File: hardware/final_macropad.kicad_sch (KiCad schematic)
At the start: 65 parts, among them J1 OLED_128x64, SW1 SW_Push, U1 ATmega32U4-A, Y1 16MHz

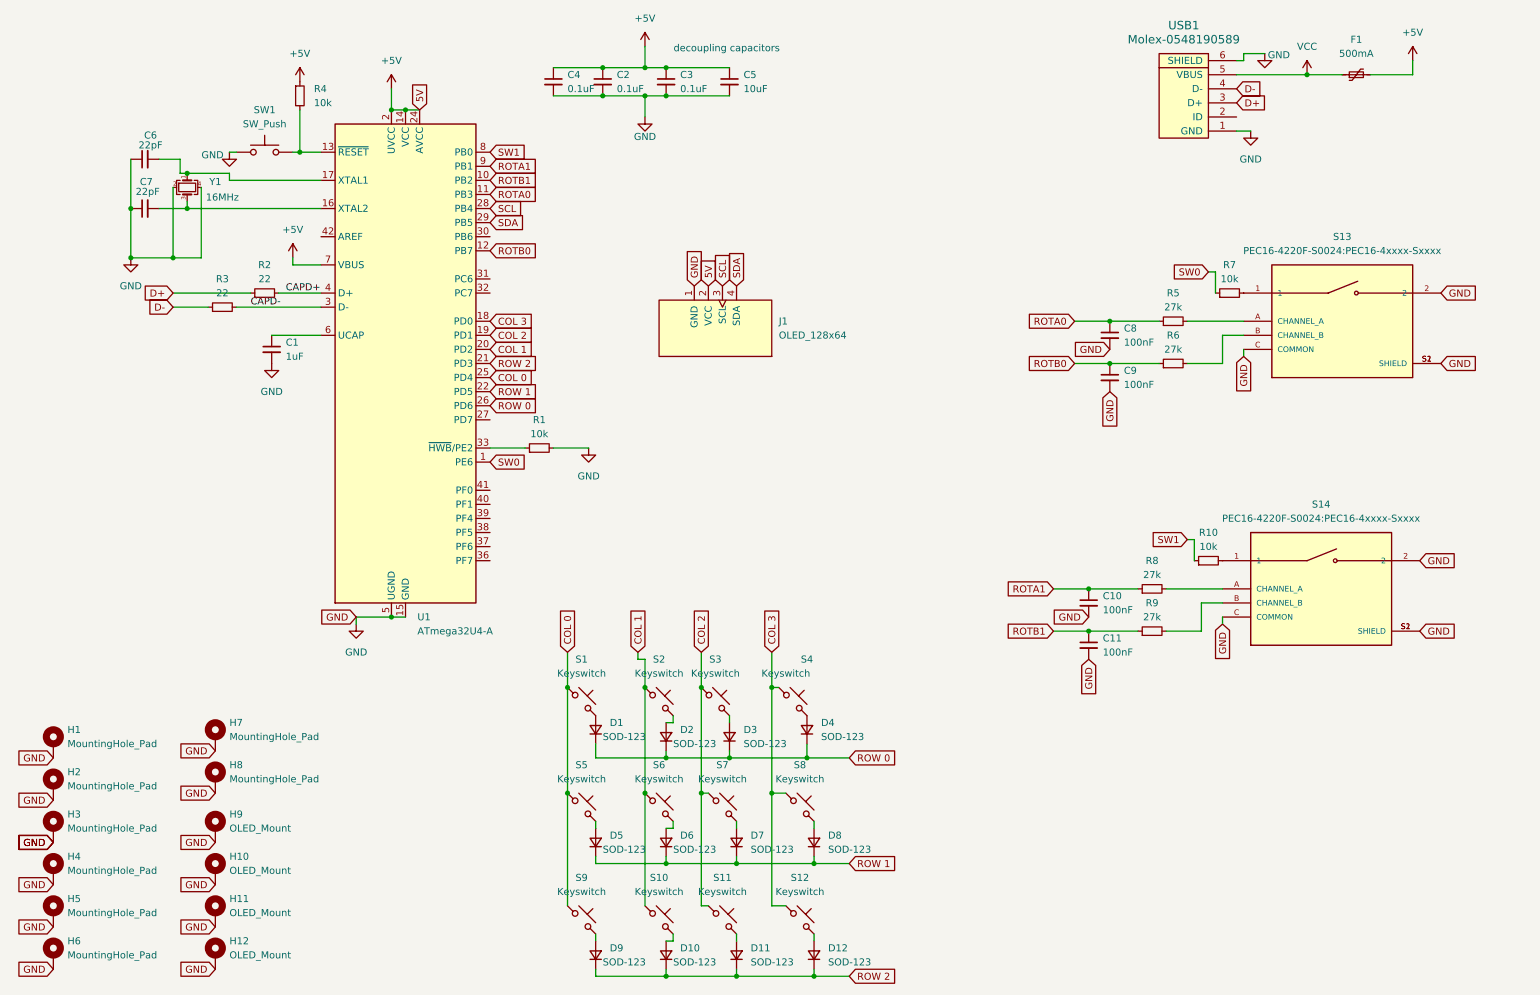
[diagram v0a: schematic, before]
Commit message: organize schematic and add USB-C and surge protector
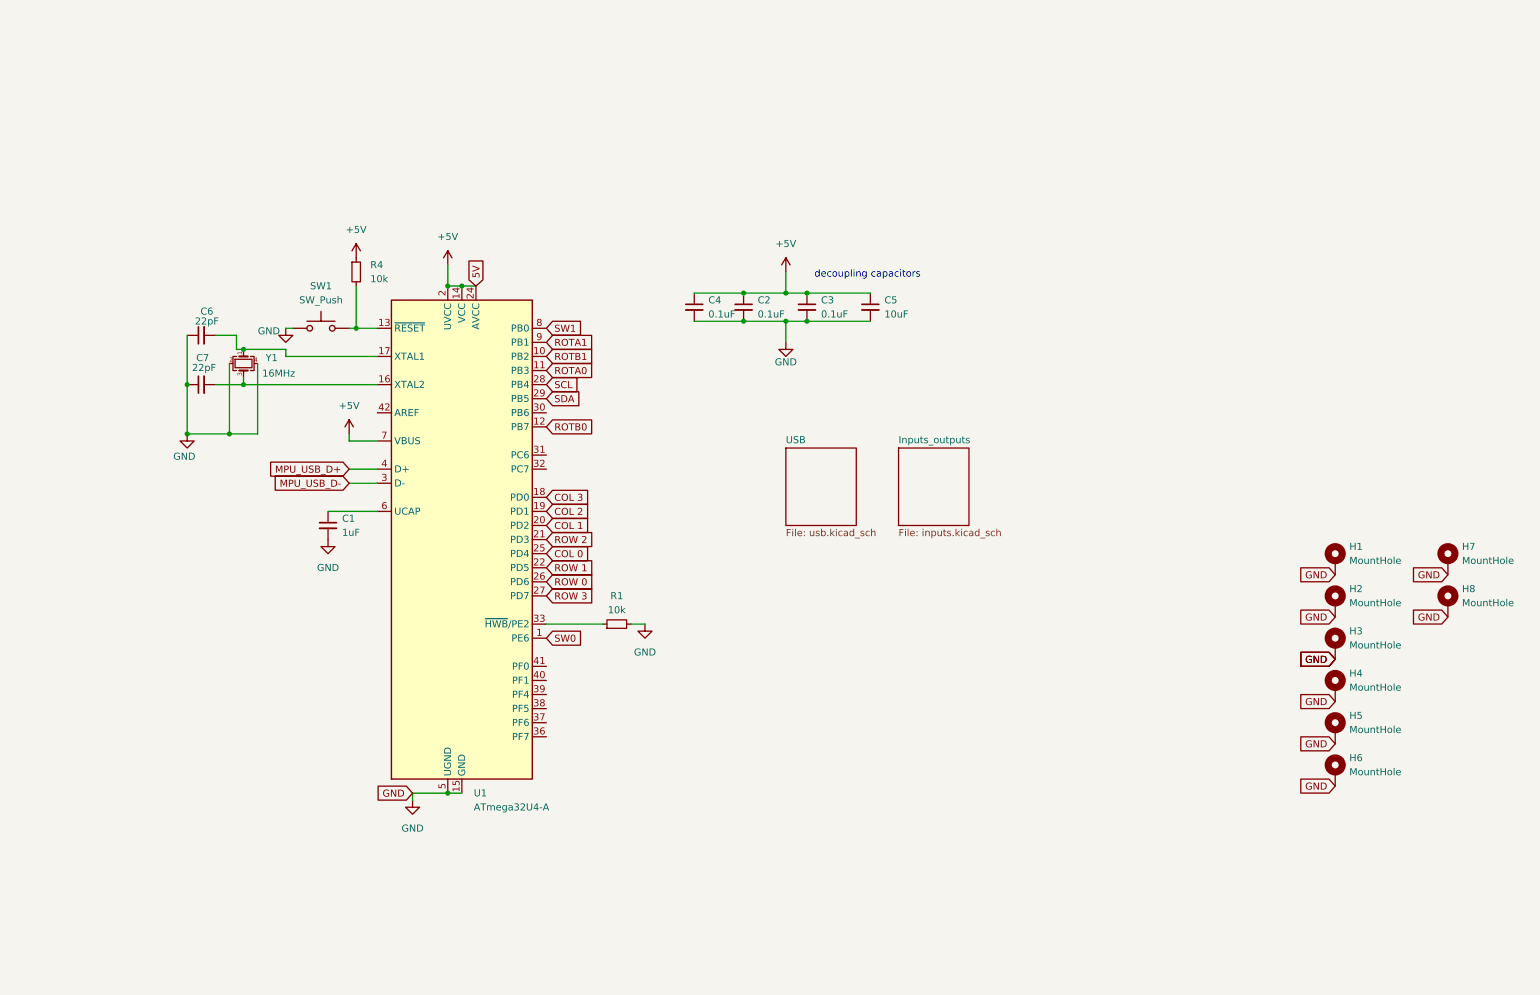
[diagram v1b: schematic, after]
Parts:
- removed C10, C11, C8, C9: 100nF, Capacitor_SMD:C_0805_2012Metric, symbol Device:C_Small
- removed D1, D10, D11, D12, D2, D3, D4, D5, D6, D7, D8, D9: SOD-123, Diode_SMD:D_SOD-123, symbol Device:D_Small
- removed F1: 500mA, Fuse:Fuse_1206_3216Metric, symbol Device:Polyfuse_Small
- removed H10, H11, H12, H9: OLED_Mount, MountingHole:MountingHole_2.2mm_M2_Pad, symbol Mechanical:MountingHole_Pad
- removed J1: OLED_128x64, ScottoKeebs_Components:OLED_128x64, symbol ScottoKeebs:OLED_128x64
- removed R10, R7: 10k, Resistor_SMD:R_0805_2012Metric, symbol Device:R_Small
- removed R2, R3: 22, Resistor_SMD:R_0402_1005Metric_Pad0.72x0.64mm_HandSolder, symbol Device:R_Small
- removed R5, R6, R8, R9: 27k, Resistor_SMD:R_0805_2012Metric, symbol Device:R_Small
- removed S1, S10, S11, S12, S2, S3, S4, S5, S6, S7, S8, S9: Keyswitch, Button_Switch_Keyboard:SW_Cherry_MX_1.00u_PCB, symbol ScottoKeebs:Placeholder_Keyswitch
- removed S13: PEC16-4220F-S0024:PEC16-4xxxx-Sxxxx, PEC16-4220F-S0024:PEC16-4xxxx-Sxxxx, symbol PEC12R-2220F-S0024:PEC12R-2220F-S0024
- removed S14: PEC16-4220F-S0024:PEC16-4xxxx-Sxxxx, kicad-footprints:PEC16-4xxxx-Sxxxx, symbol PEC12R-2220F-S0024:PEC12R-2220F-S0024
- removed USB1: Molex-0548190589, random-keyboard-parts:Molex-0548190589, symbol random-keyboard-parts:Molex-0548190589
- H1, H2, H3, H4, H5, H6, H7, H8: value MountingHole_Pad -> MountHole
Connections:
- net ROW 3: now reaches U1.27 (PD7)
- net CAPD+ renamed MPU_USB_D+
- net CAPD- renamed MPU_USB_D-
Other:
- added sheet Inputs_outputs (inputs.kicad_sch)
- added sheet USB (usb.kicad_sch)
- moved on the sheet: C1, C2, C3, C4, C5, C6, C7, H1, H2, H3, H4, H5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

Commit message: fix switches to be correct order and move diodes
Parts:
- H5, H6, H7, H8: footprint MountingHole:MountingHole_3.2mm_M3_Pad_Via -> MountingHole:MountingHole_2.2mm_M2_Pad
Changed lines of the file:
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@@
 			)
 		)
-		(property "Footprint" "MountingHole:MountingHole_3.2mm_M3_Pad_Via"
+		(property "Footprint" "MountingHole:MountingHole_2.2mm_M2_Pad"
 			(at 251.46 146.05 0)
 			(effects
@@
 			)
 		)
-		(property "Footprint" "MountingHole:MountingHole_3.2mm_M3_Pad_Via"
+		(property "Footprint" "MountingHole:MountingHole_2.2mm_M2_Pad"
 			(at 271.78 123.19 0)
 			(effects
@@
 			)
 		)
-		(property "Footprint" "MountingHole:MountingHole_3.2mm_M3_Pad_Via"
+		(property "Footprint" "MountingHole:MountingHole_2.2mm_M2_Pad"
 			(at 251.46 153.67 0)
 			(effects
@@
 			)
 		)
-		(property "Footprint" "MountingHole:MountingHole_3.2mm_M3_Pad_Via"
+		(property "Footprint" "MountingHole:MountingHole_2.2mm_M2_Pad"
 			(at 271.78 115.57 0)
 			(effects

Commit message: update BOM and reset button footprint
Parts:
- removed SW1: SW_Push, random-keyboard-parts:SKQG-1155865, symbol Switch:SW_Push
- added SW1: SKQGADE010, SKQGADE010_AAL, symbol low_profile_switch_4809-SKQGADE010:SKQGADE010
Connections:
- net GND: now also SW1.4
- net at R4.2, U1.13 (~{RESET}): now also SW1.3
- no-connect marks 0 -> 10
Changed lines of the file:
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@@
 		(color 0 0 0 0)
 	)
+	(no_connect
+		(at 109.22 134.62)
+	)
+	(no_connect
+		(at 109.22 142.24)
+	)
+	(no_connect
+		(at 109.22 139.7)
+	)
+	(no_connect
+		(at 43.18 66.04)
+	)
+	(no_connect
+		(at 109.22 99.06)
+	)
+	(no_connect
+		(at 109.22 147.32)
+	)
+	(no_connect
+		(at 68.58 66.04)
+	)
+	(no_connect
+		(at 109.22 96.52)
+	)
+	(no_connect
+		(at 109.22 137.16)
+	)
+	(no_connect
+		(at 109.22 144.78)
+	)
 	(wire
 		(pts
@@
 	(wire
 		(pts
+			(xy 71.12 73.66) (xy 71.12 63.5)
+		)
+		(stroke
+			(width 0)
+			(type default)
+		)
+	)
+	(wire
+		(pts
 			(xy 49.53 83.82) (xy 54.61 83.82)
 		)
@@
 	(wire
 		(pts
-			(xy 73.66 73.66) (xy 74.93 73.66)
+			(xy 71.12 73.66) (xy 74.93 73.66)
 		)
 		(stroke
@@
 	(wire
 		(pts
+			(xy 71.12 63.5) (xy 68.58 63.5)
+		)
+		(stroke
+			(width 0)
+			(type default)
+		)
+	)
+	(wire
+		(pts
 			(xy 62.23 78.74) (xy 62.23 77.47)
 		)
@@
 	(wire
 		(pts
-			(xy 63.5 73.66) (xy 62.23 73.66)
-		)
-		(stroke
-			(width 0)
-			(type default)
-		)
-	)
-	(wire
-		(pts
 			(xy 85.09 158.75) (xy 85.09 157.48)
 		)
@@
 		(pts
 			(xy 62.23 78.74) (xy 78.74 78.74)
+		)
+		(stroke
+			(width 0)
+			(type default)
+		)
+	)
+	(wire
+		(pts
+			(xy 40.64 63.5) (xy 43.18 63.5)
 		)
 		(stroke
@@
 	(symbol
 		(lib_id "power:GND")
-		(at 62.23 73.66 0)
+		(at 40.64 63.5 0)
 		(unit 1)
 		(exclude_from_sim no)
@@
 		(dnp no)
 		(property "Reference" "#PWR09"
-			(at 62.23 80.01 0)
+			(at 40.64 69.85 0)
 			(effects
 				(font
@@
 		)
 		(property "Value" "GND"
-			(at 59.182 74.168 0)
+			(at 37.592 64.008 0)
 			(effects
 				(font
@@
 		)
 		(property "Footprint" ""
-			(at 62.23 73.66 0)
+			(at 40.64 63.5 0)
 			(effects
 				(font
@@
 		)
 		(property "Datasheet" ""
-			(at 62.23 73.66 0)
+			(at 40.64 63.5 0)
 			(effects
 				(font
@@
 		)
 		(property "Description" "Power symbol creates a global label with name \"GND\" , ground"
-			(at 62.23 73.66 0)
+			(at 40.64 63.5 0)
 			(effects
 				(font
@@
 	)
 	(symbol
-		(lib_id "Switch:SW_Push")
-		(at 68.58 73.66 0)
-		(unit 1)
-		(exclude_from_sim no)
-		(in_bom yes)
-		(on_board yes)
-		(dnp no)
-		(fields_autoplaced yes)
-		(property "Reference" "SW1"
-			(at 68.58 66.04 0)
-			(effects
-				(font
-					(size 1.27 1.27)
-				)
-			)
-		)
-		(property "Value" "SW_Push"
-			(at 68.58 68.58 0)
-			(effects
-				(font
-					(size 1.27 1.27)
-				)
-			)
-		)
-		(property "Footprint" "random-keyboard-parts:SKQG-1155865"
-			(at 68.58 68.58 0)
-			(effects
-				(font
-					(size 1.27 1.27)
-				)
-				(hide yes)
-			)
-		)
-		(property "Datasheet" "~"
-			(at 68.58 68.58 0)
-			(effects
-				(font
-					(size 1.27 1.27)
-				)
-				(hide yes)
-			)
-		)
-		(property "Description" "Push button switch, generic, two pins"
-			(at 68.58 73.66 0)
-			(effects
-				(font
-					(size 1.27 1.27)
-				)
-				(hide yes)
-			)
-		)
-		(pin "1"
-		)
-		(pin "2"
-		)
-		(instances
-			(project "final_macropad"
-				(path "/5d184ef1-151a-4114-9d49-de87ac832ddf"
-					(reference "SW1")
-					(unit 1)
-				)
-			)
-		)
-	)
-	(symbol
 		(lib_id "Mechanical:MountingHole_Pad")
 		(at 251.46 146.05 0)
@@
 					(unit 1)
 				)
+			)
+		)
+	)
+	(symbol
+		(lib_id "low_profile_switch_4809-SKQGADE010:SKQGADE010")
+		(at 68.58 66.04 180)
+		(unit 1)
+		(exclude_from_sim no)
+		(in_bom yes)
+		(on_board yes)
+		(dnp no)
+		(fields_autoplaced yes)
+		(property "Reference" "SW1"
+			(at 55.88 55.88 0)
+			(effects
+				(font
+					(size 1.524 1.524)
+				)
+			)
+		)
+		(property "Value" "SKQGADE010"
+			(at 55.88 58.42 0)
+			(effects
+				(font
+					(size 1.524 1.524)
+				)
+			)
+		)
+		(property "Footprint" "SKQGADE010_AAL"
+			(at 68.58 66.04 0)
+			(effects
+				(font
+					(size 1.27 1.27)
+					(italic yes)
+				)
+				(hide yes)
+			)
+		)
+		(property "Datasheet" "SKQGADE010"
+			(at 68.58 66.04 0)
+			(effects
+				(font
+					(size 1.27 1.27)
+					(italic yes)
+				)
+				(hide yes)
+			)
+		)
+		(property "Description" ""
+			(at 68.58 66.04 0)
+			(effects
+				(font
+					(size 1.27 1.27)
+				)
+				(hide yes)
+			)
+		)
+		(pin "1"
+		)
+		(pin "3"
+		)
+		(pin "2"
+		)
+		(pin "4"
+		)
+		(instances
+			(project ""
+				(path "/5d184ef1-151a-4114-9d49-de87ac832ddf"
+					(reference "SW1")
+					(unit 1)
+				)

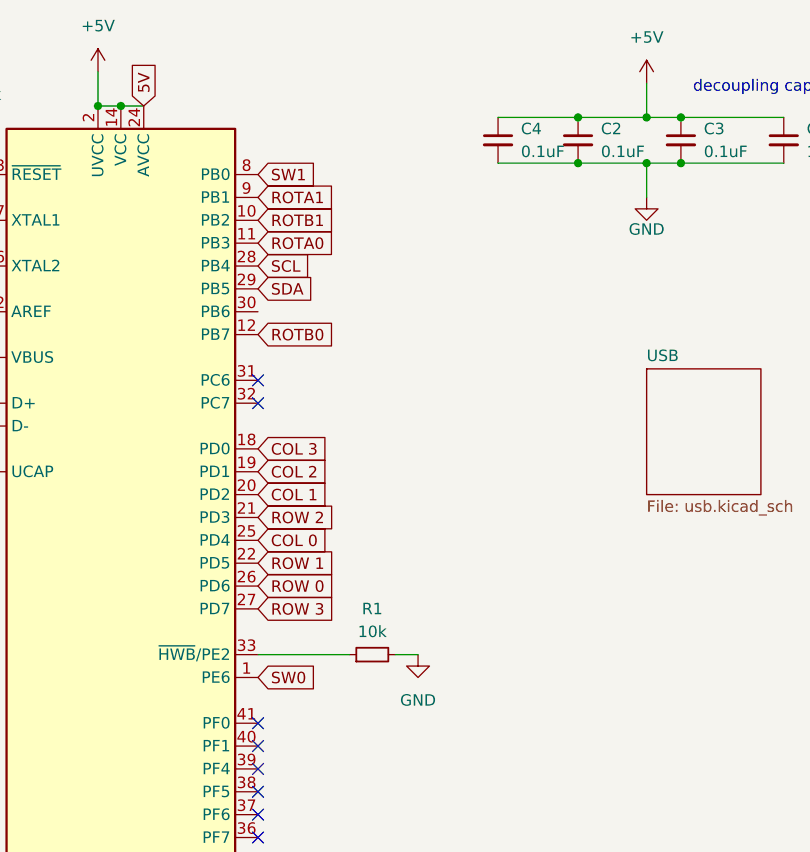
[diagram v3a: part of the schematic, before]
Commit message: rotate MCU, route reset button, crystal, and OLED
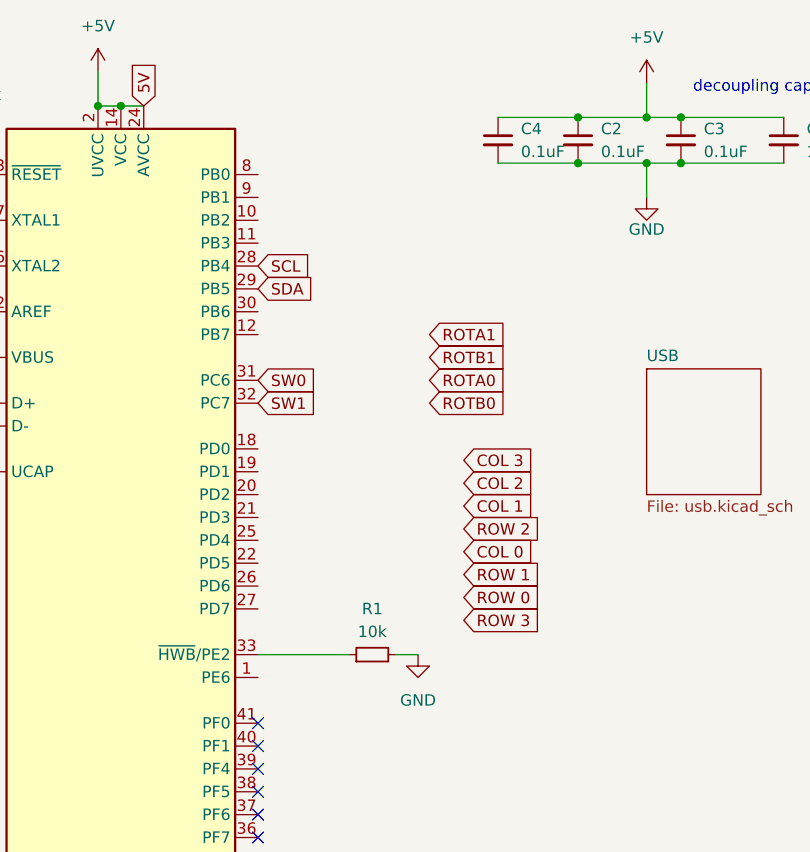
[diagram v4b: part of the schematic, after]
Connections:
- net COL 0: no longer U1.25 (PD4)
- net COL 1: no longer U1.20 (PD2)
- net COL 2: no longer U1.19 (PD1)
- net COL 3: no longer U1.18 (PD0)
- net ROTA0: no longer U1.11 (PB3)
- net ROTA1: no longer U1.9 (PB1)
- net ROTB0: no longer U1.12 (PB7)
- net ROTB1: no longer U1.10 (PB2)
- net ROW 0: no longer U1.26 (PD6)
- net ROW 1: no longer U1.22 (PD5)
- net ROW 2: no longer U1.21 (PD3)
- net ROW 3: no longer U1.27 (PD7)
- net SW0: now also U1.31 (PC6); no longer U1.1 (PE6)
- net SW1: now also U1.32 (PC7); no longer U1.8 (PB0)
- no-connect marks 10 -> 8

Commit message: Finish rerouting
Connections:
- net COL 0: now also U1.32 (PC7)
- net COL 1: now also U1.29 (PB5)
- net COL 2: now also U1.27 (PD7)
- net COL 3: now also U1.26 (PD6)
- net ROTA0: now also U1.18 (PD0)
- net ROTA1: now also U1.19 (PD1)
- net ROTB0: now also U1.20 (PD2)
- net ROTB1: now also U1.21 (PD3)
- net ROW 0: now also U1.31 (PC6)
- net ROW 1: now also U1.30 (PB6)
- net ROW 2: now also U1.28 (PB4)
- net ROW 3: now also U1.41 (PF0)
- net SCL: now also U1.8 (PB0); no longer U1.28 (PB4)
- net SDA: now also U1.9 (PB1); no longer U1.29 (PB5)
- net SW0: now also U1.12 (PB7); no longer U1.31 (PC6)
- net SW1: now also U1.11 (PB3); no longer U1.32 (PC7)
- no-connect marks 8 -> 13

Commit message: build gerber files
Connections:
- no-connect marks 13 -> 12
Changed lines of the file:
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@@
-	)
-	(no_connect
-		(at 116.84 115.57)
 	)
 	(no_connect
